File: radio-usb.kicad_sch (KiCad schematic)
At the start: 230 parts, among them J1 miniUSB, J10 Conn_Coaxial, J11 ACJS-MHDRM, J12 ACJS-MHDRM, J2 Barrel_Jack, J3 15EDGRC-3.5-03P-14, J4 DB9_Female, J5 EEP_EN, J6 Mini-DIN-6, J7 EDAC 690-008-221-904, J8 DB9_Male, J9 Conn_Coaxial, Q1 BC846C, Q2 BC846, Q3 BC846, Q4 BC846, Q5 BC856, SW1 SW_Push_DPDT, SW2 SW_SPDT, SW3 SW_SPDT, SW4 SW_DIP_x04, SW5 SW_DIP_x04, SW6 SW_DPDT_x2, SW7 SW_SPDT, U1 L7805, U10 AP2171W, U11 TLP2662, U12 TLP2662, U13 MAX3232, U14 93CxxC, U15 PCM2902, U16 MIC5209-3.6YS, U17 FT2232HL, U18 PC817, U19 CRIYCHLEY9000, U2 24LC04, U20 PC817, U21 PC817, U22 CRIYCHLEY9000, U23 LMV358, U3 APX809_810-xxSA, U4 AP22814AW5, U5 AP22814AW5, U6 USB2514B_Bi, U7 LM1117-3.3, U8 TBA 1-0511, U9 4069, X1 MAB5SH, Y1 24MHz, Y2 12MHz, Y3 12M

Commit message: daily
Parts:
- D1, D15, D16, D4, D5: footprint Capacitor_SMD:C_0805_2012Metric_Pad1.18x1.45mm_HandSolder -> LED_SMD:LED_0805_2012Metric_Pad1.15x1.40mm_HandSolder
- D6: value B0530W-7-F -> B130-13-F; footprint Diode_SMD:D_SOD-123 -> Diode_SMD:D_SMA
- U1: footprint Package_TO_SOT_THT:TO-220-3_Horizontal_TabDown -> Package_TO_SOT_THT:TO-220-3_Vertical
- U11, U12: footprint Package_SO:SOIC-8_3.9x4.9mm_P1.27mm -> Package_DIP:DIP-8_W7.62mm
- Y3: footprint Crystal:Crystal_SMD_HC49-SD_HandSoldering -> Crystal:Crystal_SMD_Abracon_ABM8G-4Pin_3.2x2.5mm
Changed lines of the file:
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@@
     (property "Reference" "D5" (id 0) (at 33.147 140.208 0))
     (property "Value" "LED_HS" (id 1) (at 33.147 141.986 0))
-    (property "Footprint" "Capacitor_SMD:C_0805_2012Metric_Pad1.18x1.45mm_HandSolder" (id 2) (at 33.147 144.526 0)
+    (property "Footprint" "LED_SMD:LED_0805_2012Metric_Pad1.15x1.40mm_HandSolder" (id 2) (at 33.147 144.526 0)
       (effects (font (size 1.27 1.27)) hide)
     )
@@
     (property "Reference" "D1" (id 0) (at 21.209 104.14 0))
     (property "Value" "LED_ACTIVE" (id 1) (at 21.209 105.918 0))
-    (property "Footprint" "Capacitor_SMD:C_0805_2012Metric_Pad1.18x1.45mm_HandSolder" (id 2) (at 21.209 108.458 0)
+    (property "Footprint" "LED_SMD:LED_0805_2012Metric_Pad1.15x1.40mm_HandSolder" (id 2) (at 21.209 108.458 0)
       (effects (font (size 1.27 1.27)) hide)
     )
@@
       (effects (font (size 1.27 1.27)) (justify right))
     )
-    (property "Footprint" "Crystal:Crystal_SMD_HC49-SD_HandSoldering" (id 2) (at 303.022 188.976 0)
+    (property "Footprint" "Crystal:Crystal_SMD_Abracon_ABM8G-4Pin_3.2x2.5mm" (id 2) (at 303.022 188.976 0)
       (effects (font (size 1.27 1.27)) hide)
     )
@@
     (property "Reference" "D4" (id 0) (at 33.147 119.38 0))
     (property "Value" "LED_HS" (id 1) (at 33.147 121.285 0))
-    (property "Footprint" "Capacitor_SMD:C_0805_2012Metric_Pad1.18x1.45mm_HandSolder" (id 2) (at 33.147 123.444 0)
+    (property "Footprint" "LED_SMD:LED_0805_2012Metric_Pad1.15x1.40mm_HandSolder" (id 2) (at 33.147 123.444 0)
       (effects (font (size 1.27 1.27)) hide)
     )
@@
     (in_bom yes) (on_board yes) (fields_autoplaced)
     (property "Reference" "D6" (id 0) (at 36.6395 174.6082 0))
-    (property "Value" "B0530W-7-F" (id 1) (at 36.6395 177.1451 0))
-    (property "Footprint" "Diode_SMD:D_SOD-123" (id 2) (at 36.322 179.578 0)
+    (property "Value" "B130-13-F" (id 1) (at 36.6395 177.1451 0))
+    (property "Footprint" "Diode_SMD:D_SMA" (id 2) (at 36.322 179.578 0)
       (effects (font (size 1.27 1.27)) hide)
     )
@@
       (effects (font (size 1.27 1.27)) (justify right))
     )
-    (property "Footprint" "Capacitor_SMD:C_0805_2012Metric_Pad1.18x1.45mm_HandSolder" (id 2) (at 322.072 136.398 0)
+    (property "Footprint" "LED_SMD:LED_0805_2012Metric_Pad1.15x1.40mm_HandSolder" (id 2) (at 322.072 136.398 0)
       (effects (font (size 1.27 1.27)) hide)
     )
@@
       (effects (font (size 1.27 1.27)) (justify right))
     )
-    (property "Footprint" "Package_SO:SOIC-8_3.9x4.9mm_P1.27mm" (id 2) (at 165.862 282.448 0)
+    (property "Footprint" "Package_DIP:DIP-8_W7.62mm" (id 2) (at 165.862 282.448 0)
       (effects (font (size 1.27 1.27)) hide)
     )
@@
       (effects (font (size 1.27 1.27)) (justify right))
     )
-    (property "Footprint" "Capacitor_SMD:C_0805_2012Metric_Pad1.18x1.45mm_HandSolder" (id 2) (at 317.754 136.398 0)
+    (property "Footprint" "LED_SMD:LED_0805_2012Metric_Pad1.15x1.40mm_HandSolder" (id 2) (at 317.754 136.398 0)
       (effects (font (size 1.27 1.27)) hide)
     )
@@
     (property "Reference" "U1" (id 0) (at 52.578 173.9732 0))
     (property "Value" "L7805" (id 1) (at 52.578 176.5101 0))
-    (property "Footprint" "Package_TO_SOT_THT:TO-220-3_Horizontal_TabDown" (id 2) (at 53.213 183.388 0)
+    (property "Footprint" "Package_TO_SOT_THT:TO-220-3_Vertical" (id 2) (at 53.213 183.388 0)
       (effects (font (size 1.27 1.27) italic) (justify left) hide)
     )
@@
       (effects (font (size 1.27 1.27)) (justify left))
     )
-    (property "Footprint" "Package_SO:SOIC-8_3.9x4.9mm_P1.27mm" (id 2) (at 166.116 249.174 0)
+    (property "Footprint" "Package_DIP:DIP-8_W7.62mm" (id 2) (at 166.116 249.174 0)
       (effects (font (size 1.27 1.27)) hide)
     )
@@
     )
     (path "/2b46b8ce-fbd7-4832-b43f-7c5a2c83b3b3"
-      (reference "D1") (unit 1) (value "LED_ACTIVE") (footprint "Capacitor_SMD:C_0805_2012Metric_Pad1.18x1.45mm_HandSolder")
+      (reference "D1") (unit 1) (value "LED_ACTIVE") (footprint "LED_SMD:LED_0805_2012Metric_Pad1.15x1.40mm_HandSolder")
     )
     (path "/3cace1e3-a8c5-42ce-a715-b378a2eba614"
@@
     )
     (path "/63c9edc1-4842-45dd-ba65-1cd2549161e5"
-      (reference "D4") (unit 1) (value "LED_HS") (footprint "Capacitor_SMD:C_0805_2012Metric_Pad1.18x1.45mm_HandSolder")
+      (reference "D4") (unit 1) (value "LED_HS") (footprint "LED_SMD:LED_0805_2012Metric_Pad1.15x1.40mm_HandSolder")
     )
     (path "/25b847c5-5a9c-4c4b-b882-8c34e2ec36b1"
-      (reference "D5") (unit 1) (value "LED_HS") (footprint "Capacitor_SMD:C_0805_2012Metric_Pad1.18x1.45mm_HandSolder")
+      (reference "D5") (unit 1) (value "LED_HS") (footprint "LED_SMD:LED_0805_2012Metric_Pad1.15x1.40mm_HandSolder")
     )
     (path "/7c5a4093-681c-40c1-8700-d3e8549580ef"
-      (reference "D6") (unit 1) (value "B0530W-7-F") (footprint "Diode_SMD:D_SOD-123")
+      (reference "D6") (unit 1) (value "B130-13-F") (footprint "Diode_SMD:D_SMA")
     )
     (path "/d8b61dc3-76da-4f21-9f81-099f2a4e9991"
@@
     )
     (path "/b2315279-acc3-4d1c-ac73-aa85b2d0ceeb"
-      (reference "D15") (unit 1) (value "LED") (footprint "Capacitor_SMD:C_0805_2012Metric_Pad1.18x1.45mm_HandSolder")
+      (reference "D15") (unit 1) (value "LED") (footprint "LED_SMD:LED_0805_2012Metric_Pad1.15x1.40mm_HandSolder")
     )
     (path "/7dfad80a-5266-4129-aa19-302c1c8b44e7"
-      (reference "D16") (unit 1) (value "LED") (footprint "Capacitor_SMD:C_0805_2012Metric_Pad1.18x1.45mm_HandSolder")
+      (reference "D16") (unit 1) (value "LED") (footprint "LED_SMD:LED_0805_2012Metric_Pad1.15x1.40mm_HandSolder")
     )
     (path "/247e4700-e25c-4aad-b923-a065ffaa5a35"
@@
     )
     (path "/bf98314c-b779-4344-9dda-f575b10bf91f"
-      (reference "U1") (unit 1) (value "L7805") (footprint "Package_TO_SOT_THT:TO-220-3_Horizontal_TabDown")
+      (reference "U1") (unit 1) (value "L7805") (footprint "Package_TO_SOT_THT:TO-220-3_Vertical")
     )
     (path "/de4a30dd-68b8-4e4c-827c-978f5ff68017"
@@
     )
     (path "/812829ac-2d71-4ef3-b373-fa97149936e4"
-      (reference "U11") (unit 1) (value "TLP2662") (footprint "Package_SO:SOIC-8_3.9x4.9mm_P1.27mm")
+      (reference "U11") (unit 1) (value "TLP2662") (footprint "Package_DIP:DIP-8_W7.62mm")
     )
     (path "/f30d3777-688f-46fd-97e3-050deb5e05e3"
-      (reference "U12") (unit 1) (value "TLP2662") (footprint "Package_SO:SOIC-8_3.9x4.9mm_P1.27mm")
+      (reference "U12") (unit 1) (value "TLP2662") (footprint "Package_DIP:DIP-8_W7.62mm")
     )
     (path "/9d74757b-c757-4993-adda-0223d46e47a4"
@@
     )
     (path "/61e59ec1-3a44-4a56-934d-cfbbd0a442a5"
-      (reference "Y3") (unit 1) (value "12M") (footprint "Crystal:Crystal_SMD_HC49-SD_HandSoldering")
+      (reference "Y3") (unit 1) (value "12M") (footprint "Crystal:Crystal_SMD_Abracon_ABM8G-4Pin_3.2x2.5mm")
     )
   )

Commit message: everything but audio codec
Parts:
- removed R19: 10k, Resistor_SMD:R_0805_2012Metric_Pad1.20x1.40mm_HandSolder, symbol Device:R
- added C1: 100n, Capacitor_SMD:C_0805_2012Metric_Pad1.18x1.45mm_HandSolder, symbol Device:C
- added C19: 100u, Capacitor_Tantalum_SMD:CP_EIA-3528-21_Kemet-B_Pad1.50x2.35mm_HandSolder, symbol Device:C_Polarized
- added C54, C56: 22n, Capacitor_SMD:C_0805_2012Metric_Pad1.18x1.45mm_HandSolder, symbol Device:C
- added R20: 0R68, Resistor_SMD:R_1206_3216Metric_Pad1.30x1.75mm_HandSolder, symbol Device:R
- added R58, R60: 16R, Resistor_SMD:R_0805_2012Metric_Pad1.20x1.40mm_HandSolder, symbol Device:R
- C15: renamed from C14; footprint Capacitor_THT:CP_Radial_D10.0mm_P5.00mm -> Capacitor_THT:CP_Radial_D5.0mm_P2.50mm
- C16: renamed from C15; value 10u -> 22u
- C18: renamed from C17; value 10u -> 22u
- C20: renamed from C18; value 10u -> 22u
- C23: renamed from C21; value 10u -> 22u
- C24: renamed from C22; footprint Capacitor_SMD:C_0805_2012Metric_Pad1.18x1.45mm_HandSolder -> Capacitor_SMD:C_0603_1608Metric_Pad1.08x0.95mm_HandSolder
- C29: renamed from C27; footprint Capacitor_SMD:C_0805_2012Metric_Pad1.18x1.45mm_HandSolder -> Capacitor_SMD:C_0603_1608Metric_Pad1.08x0.95mm_HandSolder
- C3: renamed from C2; footprint Capacitor_Tantalum_SMD:CP_EIA-3216-18_Kemet-A_Pad1.58x1.35mm_HandSolder -> Capacitor_Tantalum_SMD:CP_EIA-6032-28_Kemet-C_Pad2.25x2.35mm_HandSolder
- C32: renamed from C30; footprint Capacitor_SMD:C_0805_2012Metric_Pad1.18x1.45mm_HandSolder -> Capacitor_SMD:C_0603_1608Metric_Pad1.08x0.95mm_HandSolder
- C33: renamed from C31; footprint Capacitor_SMD:C_0805_2012Metric_Pad1.18x1.45mm_HandSolder -> Capacitor_SMD:C_0603_1608Metric_Pad1.08x0.95mm_HandSolder
- C62: renamed from C58; value 100u -> 220u; footprint Capacitor_THT:CP_Radial_D10.0mm_P5.00mm -> Capacitor_THT:CP_Radial_D6.3mm_P2.50mm; DESCRIPTION UBT1H101MPD8 NICHICON -> EEUFR1C221 PANASONIC
- C63: renamed from C59; value 100u -> 220u; footprint Capacitor_THT:CP_Radial_D10.0mm_P5.00mm -> Capacitor_THT:CP_Radial_D6.3mm_P2.50mm; DESCRIPTION UBT1H101MPD8 NICHICON -> EEUFR1C221 PANASONIC
- R17: footprint Resistor_SMD:R_0805_2012Metric_Pad1.20x1.40mm_HandSolder -> Resistor_SMD:R_0603_1608Metric_Pad0.98x0.95mm_HandSolder
- U1: footprint Package_TO_SOT_THT:TO-220-3_Vertical -> Package_TO_SOT_THT:TO-220-3_Horizontal_TabDown
- U13: footprint Package_SO:SOIC-16_3.9x9.9mm_P1.27mm -> Package_SO:TSSOP-16_4.4x5mm_P0.65mm
- U23: footprint Package_SO:SOIC-8_3.9x4.9mm_P1.27mm -> Package_SO:TSSOP-8_4.4x3mm_P0.65mm
- U9: footprint Package_SO:SOIC-14_3.9x8.7mm_P1.27mm -> Package_SO:TSSOP-14_4.4x5mm_P0.65mm
- renumbered C9 to C10, C10 to C11, C11 to C12, C12 to C13, C13 to C14, C16 to C17, C1 to C2, C20 to C21, C19 to C22, C23 to C25, C24 to C26, C25 to C27, C26 to C28, C28 to C30, C29 to C31, C32 to C34, C33 to C35, C34 to C36, C35 to C37, C36 to C38, C37 to C39, C3 to C4, C38 to C40, C39 to C41, C40 to C42, C41 to C43, C42 to C44, C43 to C45, C44 to C46, C45 to C47, C46 to C48, C47 to C49, C4 to C5, C48 to C50, C49 to C51, C50 to C52, C51 to C53, C52 to C55, C53 to C57, C54 to C58, C55 to C59, C5 to C6, C56 to C60, C57 to C61, C60 to C64, C6 to C7, C7 to C8, C8 to C9, D6 to D4, D4 to D5, D5 to D6, J2 to J1, J1 to J2, R20 to R19, R44 to R42, R42 to R43, R43 to R44, R51 to R47, R47 to R48, R48 to R49, R49 to R50, R50 to R51, R58 to R59, R59 to R61, R60 to R62, R61 to R63, R62 to R64, R63 to R65, R64 to R66, R65 to R67, R66 to R68, R67 to R69, R68 to R70, R69 to R71, R70 to R72, R71 to R73, R72 to R74, R73 to R75, R74 to R76, R75 to R77, R76 to R78, R77 to R79
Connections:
- net +12V: now also C1.1
- net AUD_OUT_LEFT: now also C54.2
- net AUD_OUT_RIGHT: now also C56.2
- net GND: now also C1.2, R20.1, R58.1, R60.1
- net at C18.1, L2.2, U8.2 (+VIN): now also C19.1
- net 5VD12: now reaches C10.1, C8.1, U1.3 (OUT), U4.4 (EN), U4.5 (IN)
- new net: C56.1, R60.2
- new net: C54.1, R58.2
- new net: C19.2, R20.2
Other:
- moved on the sheet: C20, C22, C23, D4, F1, J1, L3, U8

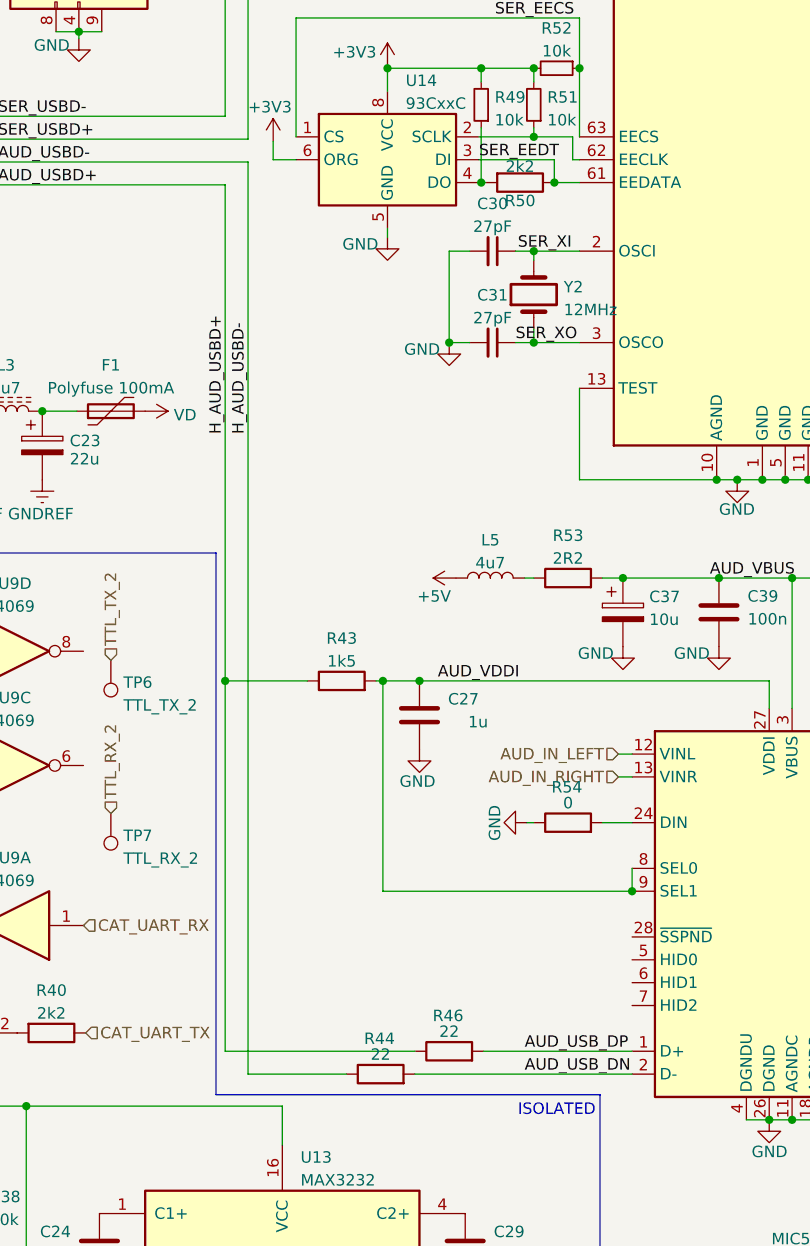
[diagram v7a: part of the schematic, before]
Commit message: some components around audio codec
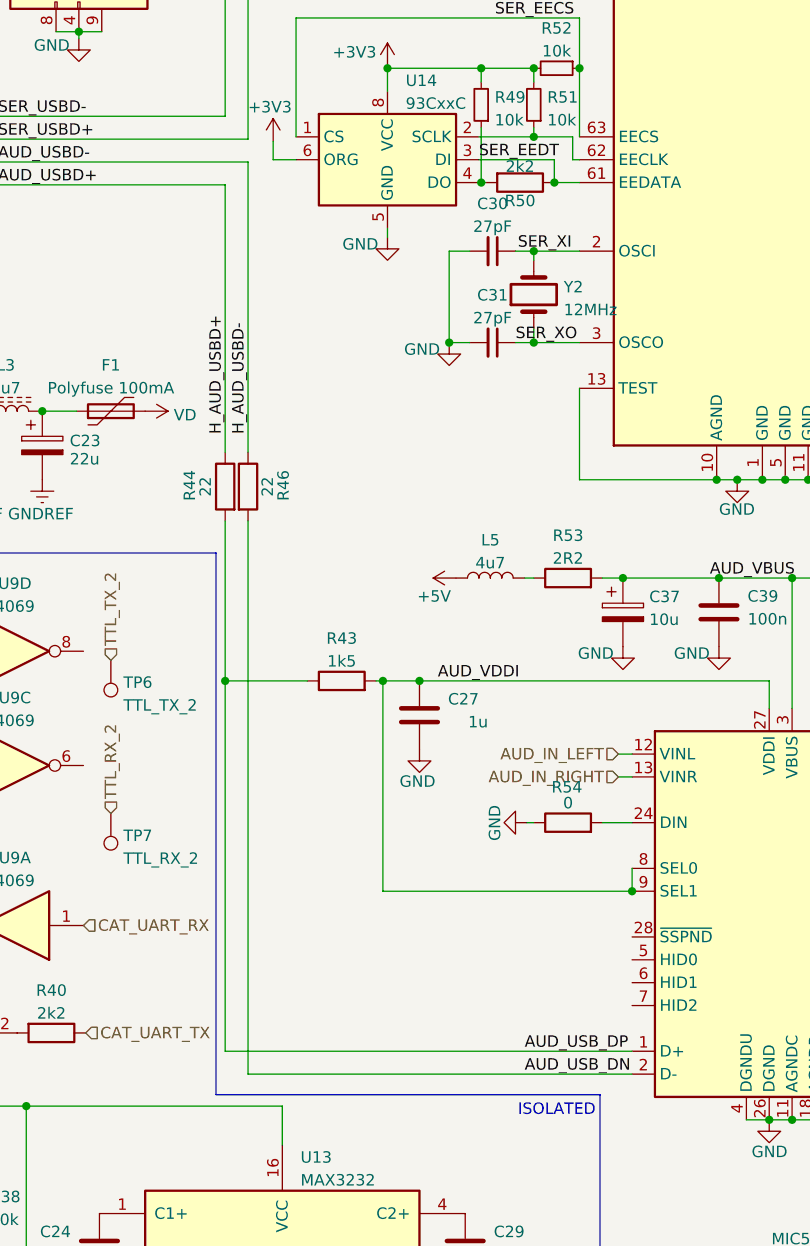
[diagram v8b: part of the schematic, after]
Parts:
- U18, U20, U21: footprint Package_DIP:DIP-4_W7.62mm -> Package_DIP:SMDIP-4_W7.62mm
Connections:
- net AUD_USB_DN: now also R46.2; no longer R44.2
- net AUD_USB_DP: now also R43.1, R44.2; no longer R46.2
- net H_AUD_USBD+: now also R44.1; no longer R43.1, R46.1
- net H_AUD_USBD-: now also R46.1; no longer R44.1
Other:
- moved on the sheet: R44, R46
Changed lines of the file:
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@@
   (junction (at 95.25 44.958) (diameter 0) (color 0 0 0 0)
   )
+  (junction (at 213.614 164.338) (diameter 0) (color 0 0 0 0)
+  )
   (junction (at 218.948 42.926) (diameter 0) (color 0 0 0 0)
   )
@@
   (junction (at 357.632 112.776) (diameter 0) (color 0 0 0 0)
   )
-  (junction (at 213.614 164.338) (diameter 0) (color 0 0 0 0)
-  )
   (junction (at 310.134 232.664) (diameter 0) (color 0 0 0 0)
   )
@@
     (stroke (width 0) (type default) (color 0 0 0 0))
   )
-  (wire (pts (xy 213.614 109.22) (xy 213.614 164.338))
+  (wire (pts (xy 213.614 146.558) (xy 213.614 164.338))
+    (stroke (width 0) (type default) (color 0 0 0 0))
+  )
+  (wire (pts (xy 213.614 109.22) (xy 213.614 138.938))
     (stroke (width 0) (type default) (color 0 0 0 0))
   )
@@
     (stroke (width 0) (type default) (color 0 0 0 0))
   )
+  (wire (pts (xy 216.154 106.68) (xy 216.154 138.938))
+    (stroke (width 0) (type default) (color 0 0 0 0))
+  )
   (polyline (pts (xy 369.57 54.61) (xy 407.162 54.61))
     (stroke (width 0) (type default) (color 0 0 0 0))
@@
     (stroke (width 0) (type default) (color 0 0 0 0))
   )
-  (wire (pts (xy 216.154 106.68) (xy 216.154 208.026))
-    (stroke (width 0) (type default) (color 0 0 0 0))
-  )
   (wire (pts (xy 184.912 69.342) (xy 184.912 66.802))
     (stroke (width 0) (type default) (color 0 0 0 0))
@@
     (stroke (width 0) (type default) (color 0 0 0 0))
   )
-  (wire (pts (xy 216.154 208.026) (xy 227.076 208.026))
+  (wire (pts (xy 216.154 208.026) (xy 258.826 208.026))
     (stroke (width 0) (type default) (color 0 0 0 0))
   )
@@
     (stroke (width 0) (type default) (color 0 0 0 0))
   )
-  (wire (pts (xy 213.614 205.486) (xy 234.696 205.486))
-    (stroke (width 0) (type default) (color 0 0 0 0))
-  )
   (wire (pts (xy 175.514 134.366) (xy 185.42 134.366))
     (stroke (width 0) (type default) (color 0 0 0 0))
@@
     (stroke (width 0) (type default) (color 0 0 0 0))
   )
-  (wire (pts (xy 242.316 205.486) (xy 258.826 205.486))
+  (wire (pts (xy 213.614 205.486) (xy 258.826 205.486))
     (stroke (width 0) (type default) (color 0 0 0 0))
   )
@@
     (stroke (width 0) (type default) (color 0 0 0 0))
   )
+  (wire (pts (xy 216.154 146.558) (xy 216.154 208.026))
+    (stroke (width 0) (type default) (color 0 0 0 0))
+  )
   (wire (pts (xy 77.724 31.242) (xy 87.884 31.242))
     (stroke (width 0) (type default) (color 0 0 0 0))
@@
     (stroke (width 0) (type default) (color 0 0 0 0))
   )
-  (wire (pts (xy 234.696 208.026) (xy 258.826 208.026))
-    (stroke (width 0) (type default) (color 0 0 0 0))
-  )
   (wire (pts (xy 377.19 58.674) (xy 377.19 66.294))
     (stroke (width 0) (type default) (color 0 0 0 0))
@@
     (pin "8")
   )
-  (symbol (lib_id "Device:R") (at 238.506 205.486 90) (unit 1)
+  (symbol (lib_id "Device:R") (at 216.154 142.748 0) (unit 1)
     (in_bom yes) (on_board yes)
-    (property "Reference" "R46" (id 0) (at 238.379 201.549 90))
-    (property "Value" "22" (id 1) (at 238.506 203.3071 90))
-    (property "Footprint" "Resistor_SMD:R_0603_1608Metric_Pad0.98x0.95mm_HandSolder" (id 2) (at 238.506 207.264 90)
+    (property "Reference" "R46" (id 0) (at 220.091 142.621 90))
+    (property "Value" "22" (id 1) (at 218.3329 142.748 90))
+    (property "Footprint" "Resistor_SMD:R_0603_1608Metric_Pad0.98x0.95mm_HandSolder" (id 2) (at 214.376 142.748 90)
       (effects (font (size 1.27 1.27)) hide)
     )
-    (property "Datasheet" "~" (id 3) (at 238.506 205.486 0)
+    (property "Datasheet" "~" (id 3) (at 216.154 142.748 0)
       (effects (font (size 1.27 1.27)) hide)
     )
@@
     (property "Reference" "U21" (id 0) (at 369.062 30.3362 0))
     (property "Value" "PC817" (id 1) (at 369.062 32.8731 0))
-    (property "Footprint" "Package_DIP:DIP-4_W7.62mm" (id 2) (at 363.982 42.926 0)
+    (property "Footprint" "Package_DIP:SMDIP-4_W7.62mm" (id 2) (at 363.982 42.926 0)
       (effects (font (size 1.27 1.27) italic) (justify left) hide)
     )
@@
     (property "Reference" "U20" (id 0) (at 369.062 14.0802 0))
     (property "Value" "PC817" (id 1) (at 369.062 16.6171 0))
-    (property "Footprint" "Package_DIP:DIP-4_W7.62mm" (id 2) (at 363.982 26.67 0)
+    (property "Footprint" "Package_DIP:SMDIP-4_W7.62mm" (id 2) (at 363.982 26.67 0)
       (effects (font (size 1.27 1.27) italic) (justify left) hide)
     )
@@
     (pin "2")
   )
-  (symbol (lib_id "Device:R") (at 230.886 208.026 90) (unit 1)
+  (symbol (lib_id "Device:R") (at 213.614 142.748 0) (mirror y) (unit 1)
     (in_bom yes) (on_board yes)
-    (property "Reference" "R44" (id 0) (at 230.759 204.089 90))
-    (property "Value" "22" (id 1) (at 230.886 205.8471 90))
-    (property "Footprint" "Resistor_SMD:R_0603_1608Metric_Pad0.98x0.95mm_HandSolder" (id 2) (at 230.886 209.804 90)
+    (property "Reference" "R44" (id 0) (at 209.677 142.621 90))
+    (property "Value" "22" (id 1) (at 211.4351 142.748 90))
+    (property "Footprint" "Resistor_SMD:R_0603_1608Metric_Pad0.98x0.95mm_HandSolder" (id 2) (at 215.392 142.748 90)
       (effects (font (size 1.27 1.27)) hide)
     )
-    (property "Datasheet" "~" (id 3) (at 230.886 208.026 0)
+    (property "Datasheet" "~" (id 3) (at 213.614 142.748 0)
       (effects (font (size 1.27 1.27)) hide)
     )
@@
     (property "Reference" "U18" (id 0) (at 358.902 84.1842 0))
     (property "Value" "PC817" (id 1) (at 358.902 86.7211 0))
-    (property "Footprint" "Package_DIP:DIP-4_W7.62mm" (id 2) (at 363.982 96.774 0)
+    (property "Footprint" "Package_DIP:SMDIP-4_W7.62mm" (id 2) (at 363.982 96.774 0)
       (effects (font (size 1.27 1.27) italic) (justify left) hide)
     )
@@
     )
     (path "/bc7e0b8b-6d58-4285-a34d-3747208961b0"
-      (reference "U18") (unit 1) (value "PC817") (footprint "Package_DIP:DIP-4_W7.62mm")
+      (reference "U18") (unit 1) (value "PC817") (footprint "Package_DIP:SMDIP-4_W7.62mm")
     )
     (path "/b2534dbf-3f07-412e-a157-d6f650ef36ef"
@@
     )
     (path "/804ff481-420d-45ce-8c7e-c53ca0c12cce"
-      (reference "U20") (unit 1) (value "PC817") (footprint "Package_DIP:DIP-4_W7.62mm")
+      (reference "U20") (unit 1) (value "PC817") (footprint "Package_DIP:SMDIP-4_W7.62mm")
     )
     (path "/33a78072-b48d-4b55-b5de-3617e0f1cb45"
-      (reference "U21") (unit 1) (value "PC817") (footprint "Package_DIP:DIP-4_W7.62mm")
+      (reference "U21") (unit 1) (value "PC817") (footprint "Package_DIP:SMDIP-4_W7.62mm")
     )
     (path "/f313d2cd-79cb-4376-8934-f1cf3e75cec5"
